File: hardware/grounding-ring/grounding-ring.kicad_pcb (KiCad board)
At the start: 2 copper layers, 23.6 x 33.3 mm, 1 part, among them P1 CONN_01X02

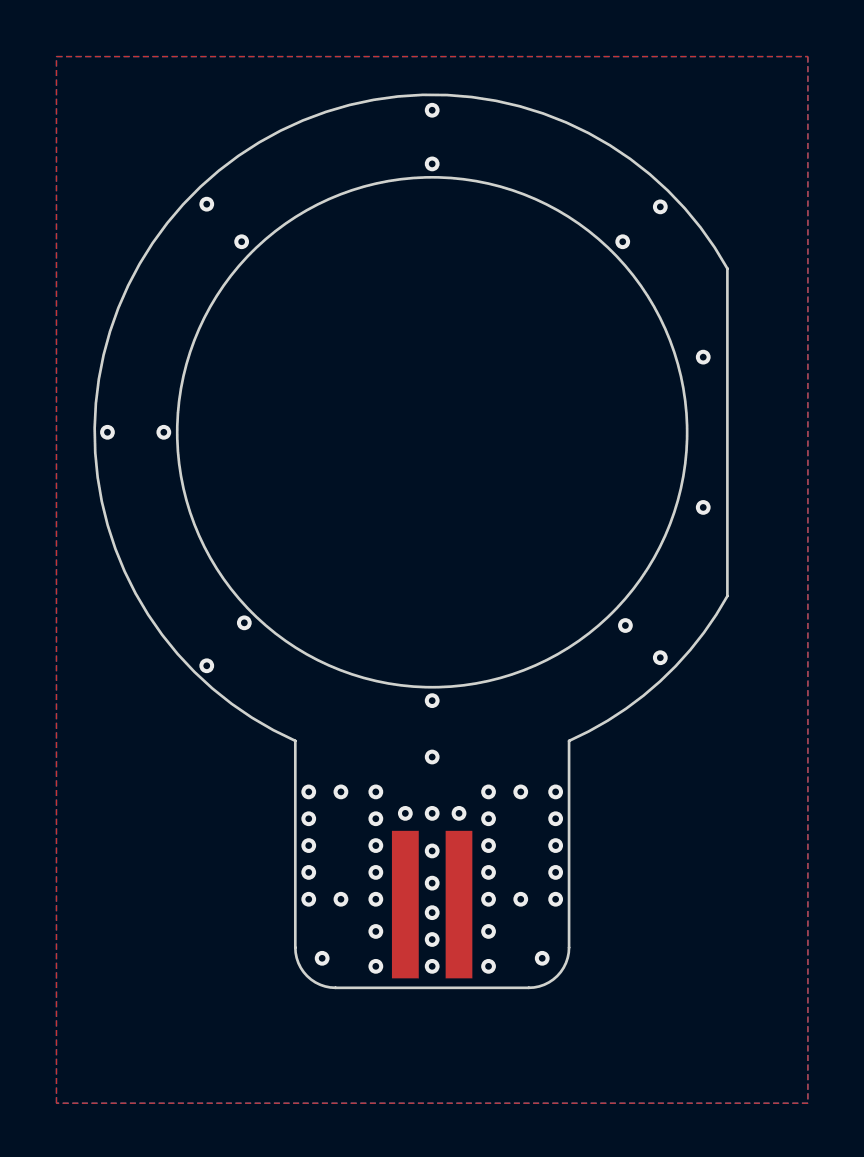
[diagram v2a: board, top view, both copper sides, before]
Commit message: grounding_ring: changed pcb layout. moved connector down by 1mm and made hole bigger by 0,1mm
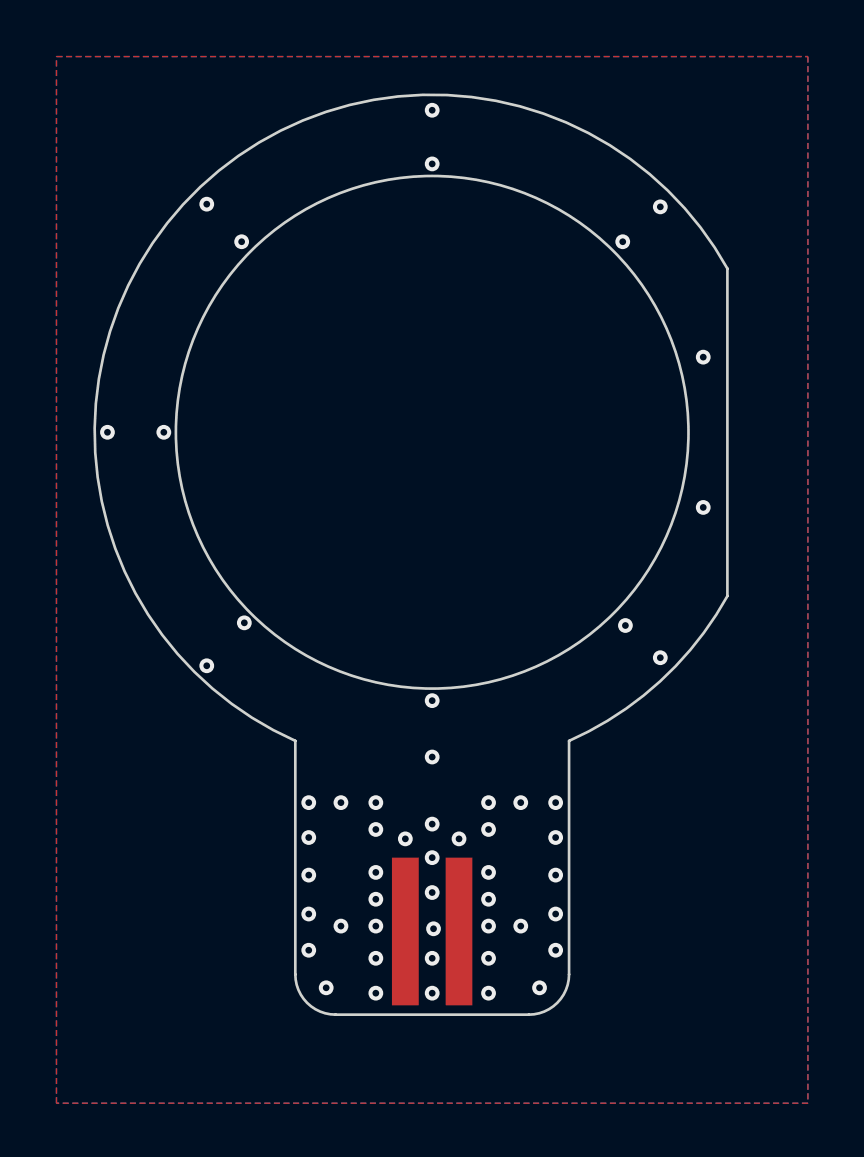
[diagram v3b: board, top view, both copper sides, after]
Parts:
- moved P1 1.00 mm to (150.0, 118.6)
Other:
- board size 23.6 x 33.3 mm -> 23.6 x 34.3 mm
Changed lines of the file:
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@@
     (36 B.SilkS user)
     (37 F.SilkS user)
-    (38 B.Mask user hide)
-    (39 F.Mask user hide)
+    (38 B.Mask user)
+    (39 F.Mask user)
     (40 Dwgs.User user)
     (41 Cmts.User user)
@@
   )
   (module kicad-libraries:JST-PH-2-SMD (layer F.Cu)
-    (at 150 117.6)
+    (at 150 118.6)
     (fp_text reference P1 (at 0.09 -3.53) (layer F.Fab)
       (effects (font (size 0.8 0.8) (thickness 0.15)))
@@
     )
   )
+  (gr_poly (pts (xy 164 111.5) (xy 155.1 111.5) (xy 154.65 111.7) (xy 153.7 112) (xy 152.8 112.25) (xy 151.7 112.5) (xy 150.65 112.6) (xy 149.6 112.6) (xy 149.2 112.55) (xy 147.95 112.45) (xy 146.7 112.15) (xy 145.5 111.75) (xy 144.9 111.5) (xy 136 111.5) (xy 136 86) (xy 164 86)) (layer B.Mask) (width 0.1))
+  (gr_poly (pts (xy 164 111.5) (xy 155.1 111.5) (xy 154.65 111.7) (xy 153.7 112) (xy 152.8 112.25) (xy 151.7 112.5) (xy 150.65 112.6) (xy 149.6 112.6) (xy 149.2 112.55) (xy 147.95 112.45) (xy 146.7 112.15) (xy 145.5 111.75) (xy 144.9 111.5) (xy 136 111.5) (xy 136 86) (xy 164 86)) (layer F.Mask) (width 0.1))
   (gr_arc (start 150 100) (end 155.099999 111.499999) (angle -37.07339432) (layer Edge.Cuts) (width 0.1))
   (gr_line (start 161 93.9) (end 161 106.1) (layer Edge.Cuts) (width 0.1))
-  (gr_arc (start 153.6 119.2) (end 153.6 120.7) (angle -90) (layer Edge.Cuts) (width 0.1))
-  (gr_arc (start 146.4 119.2) (end 144.9 119.2) (angle -90) (layer Edge.Cuts) (width 0.1))
-  (gr_arc (start 149.999999 100.600001) (end 144.9 111.5) (angle -50.14883868) (layer F.Fab) (width 0.15))
+  (gr_arc (start 153.6 120.2) (end 153.6 121.7) (angle -90) (layer Edge.Cuts) (width 0.1))
+  (gr_arc (start 146.4 120.2) (end 144.9 120.2) (angle -90) (layer Edge.Cuts) (width 0.1))
+  (gr_arc (start 150 100) (end 144.9 111.5) (angle -48.24748733) (layer F.Fab) (width 0.15))
   (gr_arc (start 150 100) (end 161 93.9) (angle -217.0733868) (layer Edge.Cuts) (width 0.1))
-  (gr_poly (pts (xy 164 113) (xy 136 113) (xy 136 86) (xy 164 86)) (layer B.Mask) (width 0.1))
-  (gr_poly (pts (xy 164 113) (xy 136 113) (xy 136 86) (xy 164 86)) (layer F.Mask) (width 0.1))
-  (gr_line (start 144.9 119.2) (end 144.9 111.5) (layer Edge.Cuts) (width 0.1))
-  (gr_line (start 153.6 120.7) (end 146.4 120.7) (layer Edge.Cuts) (width 0.1))
-  (gr_line (start 155.1 119.2) (end 155.1 111.5) (layer Edge.Cuts) (width 0.1))
-  (gr_circle (center 150 100) (end 159.5 100) (layer Edge.Cuts) (width 0.1))
+  (gr_line (start 144.9 120.2) (end 144.9 111.5) (layer Edge.Cuts) (width 0.1))
+  (gr_line (start 153.6 121.7) (end 146.4 121.7) (layer Edge.Cuts) (width 0.1))
+  (gr_line (start 155.1 120.2) (end 155.1 111.5) (layer Edge.Cuts) (width 0.1))
+  (gr_circle (center 150 100) (end 159.55 100) (layer Edge.Cuts) (width 0.1))
   (gr_text "Copyright Tinkerforge GmbH 2020.\nThis documentation describes Open Hardware and is licensed under the\nCERN OHL v. 1.1.\nYou may redistribute and modify this documentation under the terms of the\nCERN OHL v.1.1. (http://ohwr.org/cernohl). This documentation is distributed\nWITHOUT ANY EXPRESS OR IMPLIED WARRANTY, INCLUDING OF\nMERCHANTABILITY, SATISFACTORY QUALITY AND FITNESS FOR A\nPARTICULAR PURPOSE. Please see the CERN OHL v.1.1 for applicable\nconditions\n" (at 58.6 184.4) (layer F.Fab)
     (effects (font (size 1.5 1.5) (thickness 0.3)))
   )
-  (via (at 154.6 114.4) (size 0.55) (drill 0.25) (layers F.Cu B.Cu) (net 1))
-  (via (at 154.6 113.4) (size 0.55) (drill 0.25) (layers F.Cu B.Cu) (net 1))
-  (via (at 153.3 117.4) (size 0.55) (drill 0.25) (layers F.Cu B.Cu) (net 1))
-  (via (at 154.6 117.4) (size 0.55) (drill 0.25) (layers F.Cu B.Cu) (net 1))
-  (via (at 152.1 113.4) (size 0.55) (drill 0.25) (layers F.Cu B.Cu) (net 1))
+  (via (at 154.6 115.1) (size 0.55) (drill 0.25) (layers F.Cu B.Cu) (net 1))
+  (via (at 154.6 113.8) (size 0.55) (drill 0.25) (layers F.Cu B.Cu) (net 1))
+  (via (at 153.3 118.4) (size 0.55) (drill 0.25) (layers F.Cu B.Cu) (net 1))
+  (via (at 154.6 119.3) (size 0.55) (drill 0.25) (layers F.Cu B.Cu) (net 1))
+  (via (at 152.1 113.8) (size 0.55) (drill 0.25) (layers F.Cu B.Cu) (net 1))
+  (via (at 152.1 117.4) (size 0.55) (drill 0.25) (layers F.Cu B.Cu) (net 1))
+  (via (at 152.1 118.4) (size 0.55) (drill 0.25) (layers F.Cu B.Cu) (net 1))
   (via (at 152.1 116.4) (size 0.55) (drill 0.25) (layers F.Cu B.Cu) (net 1))
-  (via (at 152.1 117.4) (size 0.55) (drill 0.25) (layers F.Cu B.Cu) (net 1))
-  (via (at 152.1 115.4) (size 0.55) (drill 0.25) (layers F.Cu B.Cu) (net 1))
-  (via (at 154.6 115.4) (size 0.55) (drill 0.25) (layers F.Cu B.Cu) (net 1))
-  (via (at 152.1 114.4) (size 0.55) (drill 0.25) (layers F.Cu B.Cu) (net 1))
-  (via (at 153.3 113.4) (size 0.55) (drill 0.25) (layers F.Cu B.Cu) (net 1))
-  (via (at 154.6 116.4) (size 0.55) (drill 0.25) (layers F.Cu B.Cu) (net 1))
-  (via (at 150 114.2) (size 0.55) (drill 0.25) (layers F.Cu B.Cu) (net 1))
-  (via (at 145.4 115.4) (size 0.55) (drill 0.25) (layers F.Cu B.Cu) (net 1))
-  (via (at 145.4 114.4) (size 0.55) (drill 0.25) (layers F.Cu B.Cu) (net 1))
-  (via (at 145.4 116.4) (size 0.55) (drill 0.25) (layers F.Cu B.Cu) (net 1))
-  (via (at 145.4 113.4) (size 0.55) (drill 0.25) (layers F.Cu B.Cu) (net 1))
-  (via (at 146.6 113.4) (size 0.55) (drill 0.25) (layers F.Cu B.Cu) (net 1))
-  (via (at 147.9 113.4) (size 0.55) (drill 0.25) (layers F.Cu B.Cu) (net 1))
-  (via (at 147.9 114.4) (size 0.55) (drill 0.25) (layers F.Cu B.Cu) (net 1))
-  (via (at 147.9 115.4) (size 0.55) (drill 0.25) (layers F.Cu B.Cu) (net 1))
+  (via (at 154.6 116.5) (size 0.55) (drill 0.25) (layers F.Cu B.Cu) (net 1))
+  (via (at 152.1 114.8) (size 0.55) (drill 0.25) (layers F.Cu B.Cu) (net 1))
+  (via (at 153.3 113.8) (size 0.55) (drill 0.25) (layers F.Cu B.Cu) (net 1))
+  (via (at 154.6 117.95) (size 0.55) (drill 0.25) (layers F.Cu B.Cu) (net 1))
+  (via (at 150 114.6) (size 0.55) (drill 0.25) (layers F.Cu B.Cu) (net 1))
+  (via (at 145.4 116.5) (size 0.55) (drill 0.25) (layers F.Cu B.Cu) (net 1))
+  (via (at 145.4 115.1) (size 0.55) (drill 0.25) (layers F.Cu B.Cu) (net 1))
+  (via (at 145.4 117.95) (size 0.55) (drill 0.25) (layers F.Cu B.Cu) (net 1))
+  (via (at 145.4 113.8) (size 0.55) (drill 0.25) (layers F.Cu B.Cu) (net 1))
+  (via (at 146.6 113.8) (size 0.55) (drill 0.25) (layers F.Cu B.Cu) (net 1))
+  (via (at 147.9 113.8) (size 0.55) (drill 0.25) (layers F.Cu B.Cu) (net 1))
+  (via (at 147.9 114.8) (size 0.55) (drill 0.25) (layers F.Cu B.Cu) (net 1))
   (via (at 147.9 116.4) (size 0.55) (drill 0.25) (layers F.Cu B.Cu) (net 1))
   (via (at 147.9 117.4) (size 0.55) (drill 0.25) (layers F.Cu B.Cu) (net 1))
-  (via (at 146.6 117.4) (size 0.55) (drill 0.25) (layers F.Cu B.Cu) (net 1))
-  (via (at 145.4 117.4) (size 0.55) (drill 0.25) (layers F.Cu B.Cu) (net 1))
-  (via (at 150 115.6) (size 0.55) (drill 0.25) (layers F.Cu B.Cu) (net 1))
-  (via (at 150 116.8) (size 0.55) (drill 0.25) (layers F.Cu B.Cu) (net 1))
-  (via (at 150 117.9) (size 0.55) (drill 0.25) (layers F.Cu B.Cu) (net 1))
-  (via (at 150 118.9) (size 0.55) (drill 0.25) (layers F.Cu B.Cu) (net 1))
-  (via (at 150 119.9) (size 0.55) (drill 0.25) (layers F.Cu B.Cu) (net 1))
-  (via (at 154.1 119.6) (size 0.55) (drill 0.25) (layers F.Cu B.Cu) (net 1))
-  (via (at 152.1 119.9) (size 0.55) (drill 0.25) (layers F.Cu B.Cu) (net 1))
-  (via (at 149 114.2) (size 0.55) (drill 0.25) (layers F.Cu B.Cu) (net 1))
-  (via (at 151 114.2) (size 0.55) (drill 0.25) (layers F.Cu B.Cu) (net 1))
-  (via (at 145.9 119.6) (size 0.55) (drill 0.25) (layers F.Cu B.Cu) (net 1))
-  (via (at 152.1 118.6) (size 0.55) (drill 0.25) (layers F.Cu B.Cu) (net 1))
-  (via (at 147.9 118.6) (size 0.55) (drill 0.25) (layers F.Cu B.Cu) (net 1))
-  (via (at 147.9 119.9) (size 0.55) (drill 0.25) (layers F.Cu B.Cu) (net 1))
+  (via (at 147.9 118.4) (size 0.55) (drill 0.25) (layers F.Cu B.Cu) (net 1))
+  (via (at 146.6 118.4) (size 0.55) (drill 0.25) (layers F.Cu B.Cu) (net 1))
+  (via (at 145.4 119.3) (size 0.55) (drill 0.25) (layers F.Cu B.Cu) (net 1))
+  (via (at 150 115.85) (size 0.55) (drill 0.25) (layers F.Cu B.Cu) (net 1))
+  (via (at 150 117.15) (size 0.55) (drill 0.25) (layers F.Cu B.Cu) (net 1))
+  (via (at 150.05 118.5) (size 0.55) (drill 0.25) (layers F.Cu B.Cu) (net 1))
+  (via (at 150 119.6) (size 0.55) (drill 0.25) (layers F.Cu B.Cu) (net 1))
+  (via (at 150 120.9) (size 0.55) (drill 0.25) (layers F.Cu B.Cu) (net 1))
+  (via (at 154 120.7) (size 0.55) (drill 0.25) (layers F.Cu B.Cu) (net 1))
+  (via (at 152.1 120.9) (size 0.55) (drill 0.25) (layers F.Cu B.Cu) (net 1))
+  (via (at 149 115.15) (size 0.55) (drill 0.25) (layers F.Cu B.Cu) (net 1))
+  (via (at 151 115.15) (size 0.55) (drill 0.25) (layers F.Cu B.Cu) (net 1))
+  (via (at 146.05 120.7) (size 0.55) (drill 0.25) (layers F.Cu B.Cu) (net 1))
+  (via (at 152.1 119.6) (size 0.55) (drill 0.25) (layers F.Cu B.Cu) (net 1))
+  (via (at 147.9 119.6) (size 0.55) (drill 0.25) (layers F.Cu B.Cu) (net 1))
+  (via (at 147.9 120.9) (size 0.55) (drill 0.25) (layers F.Cu B.Cu) (net 1))
   (via (at 137.9 100) (size 0.55) (drill 0.25) (layers F.Cu B.Cu) (net 1))
   (via (at 140 100) (size 0.55) (drill 0.25) (layers F.Cu B.Cu) (net 1))

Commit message: increase pad size, outline without cutout
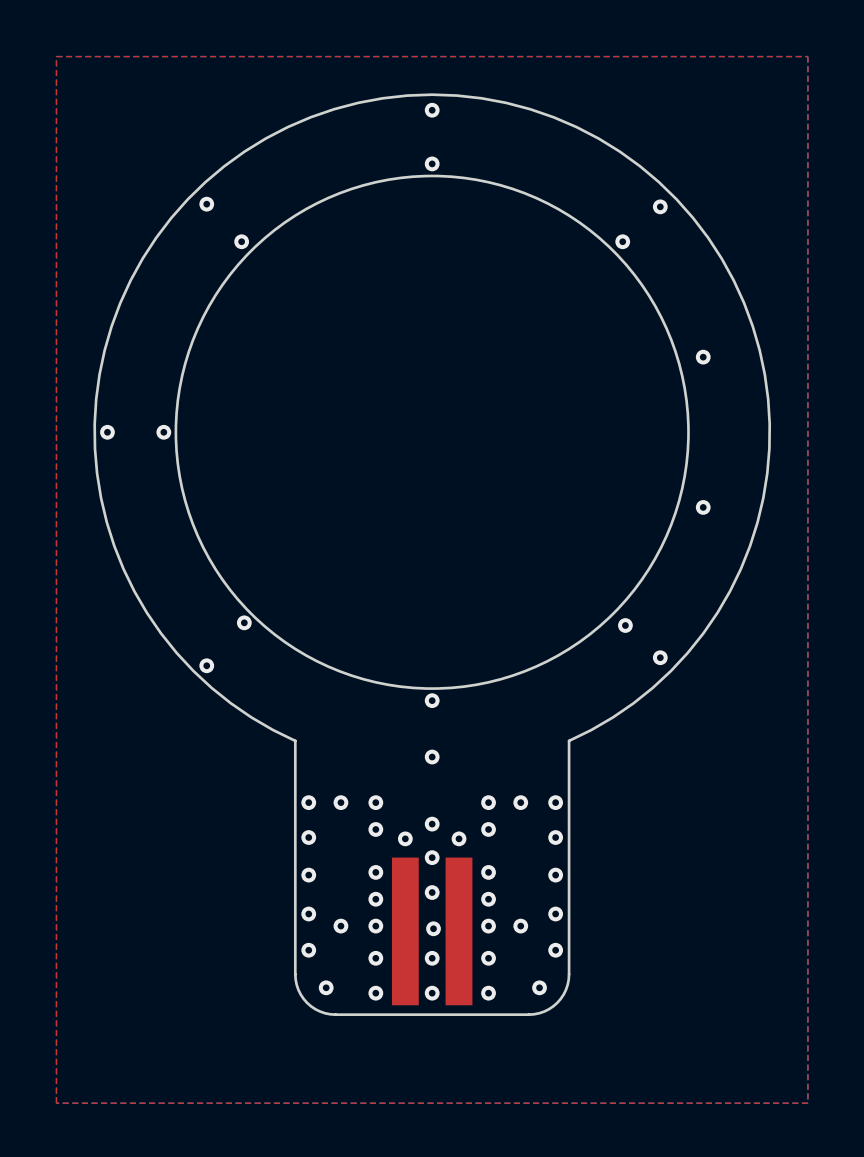
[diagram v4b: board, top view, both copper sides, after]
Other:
- board size 23.6 x 34.3 mm -> 25.2 x 34.3 mm
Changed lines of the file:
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@@
-(kicad_pcb (version 20171130) (host pcbnew 5.1.7-a382d34a8~88~ubuntu20.04.1)
+(kicad_pcb (version 20171130) (host pcbnew 5.1.12-84ad8e8a86~92~ubuntu20.04.1)
   (general
     (thickness 1.6)
-    (drawings 13)
+    (drawings 11)
     (tracks 54)
     (zones 0)
@@
     (36 B.SilkS user)
     (37 F.SilkS user)
-    (38 B.Mask user)
-    (39 F.Mask user)
+    (38 B.Mask user hide)
+    (39 F.Mask user hide)
     (40 Dwgs.User user)
     (41 Cmts.User user)
@@
     (mod_text_size 1 1)
     (mod_text_width 0.15)
-    (pad_size 1.524 1.524)
-    (pad_drill 0.762)
+    (pad_size 2 3)
+    (pad_drill 0)
     (pad_to_mask_clearance 0)
     (aux_axis_origin 150 100)
@@
       (drillshape 0)
       (scaleselection 1)
-      (outputdirectory "../../../../Schreibtisch/proto/grounding-ring/"))
+      (outputdirectory "pcb"))
   )
   (net 0 "")
@@
     (fp_line (start 3.975 -4.75) (end 3.975 0.25) (layer F.Fab) (width 0.2))
     (fp_line (start -3.975 -4.75) (end 3.975 -4.75) (layer F.Fab) (width 0.2))
-    (pad "" smd rect (at 3.4 -2.25) (size 1.6 3) (layers F.Paste F.Mask))
-    (pad "" smd rect (at -3.4 -2.25) (size 1.6 3) (layers F.Paste F.Mask))
+    (pad 1 smd rect (at -1 0) (size 1 5.5) (layers F.Cu F.Paste F.Mask)
+      (net 1 GND))
     (pad 2 smd rect (at 1 0) (size 1 5.5) (layers F.Cu F.Paste F.Mask)
       (net 1 GND))
-    (pad 1 smd rect (at -1 0) (size 1 5.5) (layers F.Cu F.Paste F.Mask)
-      (net 1 GND))
+    (pad "" smd rect (at -3.6 -2.25) (size 2 3) (layers F.Paste F.Mask))
+    (pad "" smd rect (at 3.6 -2.25) (size 2 3) (layers F.Paste F.Mask))
     (model "../3d/Connectors/B2B-PH-SM4-TB(LF)(SN).wrl"
       (at (xyz 0 0 0))
@@
   (gr_poly (pts (xy 164 111.5) (xy 155.1 111.5) (xy 154.65 111.7) (xy 153.7 112) (xy 152.8 112.25) (xy 151.7 112.5) (xy 150.65 112.6) (xy 149.6 112.6) (xy 149.2 112.55) (xy 147.95 112.45) (xy 146.7 112.15) (xy 145.5 111.75) (xy 144.9 111.5) (xy 136 111.5) (xy 136 86) (xy 164 86)) (layer B.Mask) (width 0.1))
   (gr_poly (pts (xy 164 111.5) (xy 155.1 111.5) (xy 154.65 111.7) (xy 153.7 112) (xy 152.8 112.25) (xy 151.7 112.5) (xy 150.65 112.6) (xy 149.6 112.6) (xy 149.2 112.55) (xy 147.95 112.45) (xy 146.7 112.15) (xy 145.5 111.75) (xy 144.9 111.5) (xy 136 111.5) (xy 136 86) (xy 164 86)) (layer F.Mask) (width 0.1))
-  (gr_arc (start 150 100) (end 155.099999 111.499999) (angle -37.07339432) (layer Edge.Cuts) (width 0.1))
-  (gr_line (start 161 93.9) (end 161 106.1) (layer Edge.Cuts) (width 0.1))
   (gr_arc (start 153.6 120.2) (end 153.6 121.7) (angle -90) (layer Edge.Cuts) (width 0.1))
   (gr_arc (start 146.4 120.2) (end 144.9 120.2) (angle -90) (layer Edge.Cuts) (width 0.1))
   (gr_arc (start 150 100) (end 144.9 111.5) (angle -48.24748733) (layer F.Fab) (width 0.15))
-  (gr_arc (start 150 100) (end 161 93.9) (angle -217.0733868) (layer Edge.Cuts) (width 0.1))
+  (gr_arc (start 150 100) (end 155.1 111.5) (angle -312.1674888) (layer Edge.Cuts) (width 0.1))
   (gr_line (start 144.9 120.2) (end 144.9 111.5) (layer Edge.Cuts) (width 0.1))
   (gr_line (start 153.6 121.7) (end 146.4 121.7) (layer Edge.Cuts) (width 0.1))

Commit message: GroundingRing: Upadated to Kicad 6, changed to faston connector
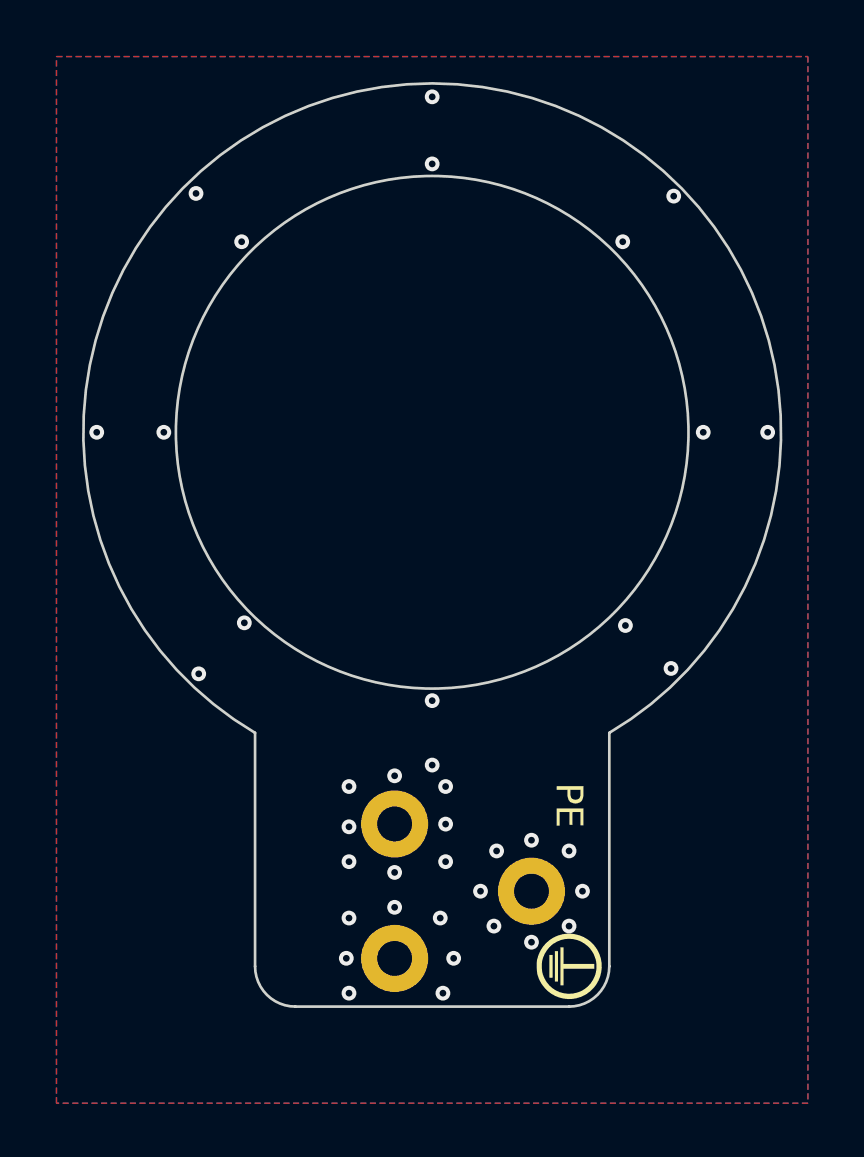
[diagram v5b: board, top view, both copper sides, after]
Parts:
- added G***: LOGO, kicad-libraries:PE_Logo, F.Cu at (155.1, 119.9)
- P1: value CONN_01X02 -> CONN_1; footprint kicad-libraries:JST-PH-2-SMD -> kicad-libraries:36-4910
- moved P1 2.05 mm to (148.6, 117.1), turned to 90 degrees
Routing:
- net GND: vias 54 -> 39
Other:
- board size 25.2 x 34.3 mm -> 26 x 34.4 mm
- net class Default removed
- board text added: "G.R. 1.1"
- board text added: "PE"
